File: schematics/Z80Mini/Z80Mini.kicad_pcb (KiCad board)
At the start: 2 copper layers, 194.3 x 105.4 mm, 50 parts, among them J1 Conn_02x20_Odd_Even, J3 USB_B_Micro, J4 Conn_02x10_Counter_Clockwise, SW1 RESET, SW2 SW_DIP_x04, U1 Z80CPU, U2 TC55257CPI, U3 AT28C64B-15PU, U4 74LS32, U5 74HC14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

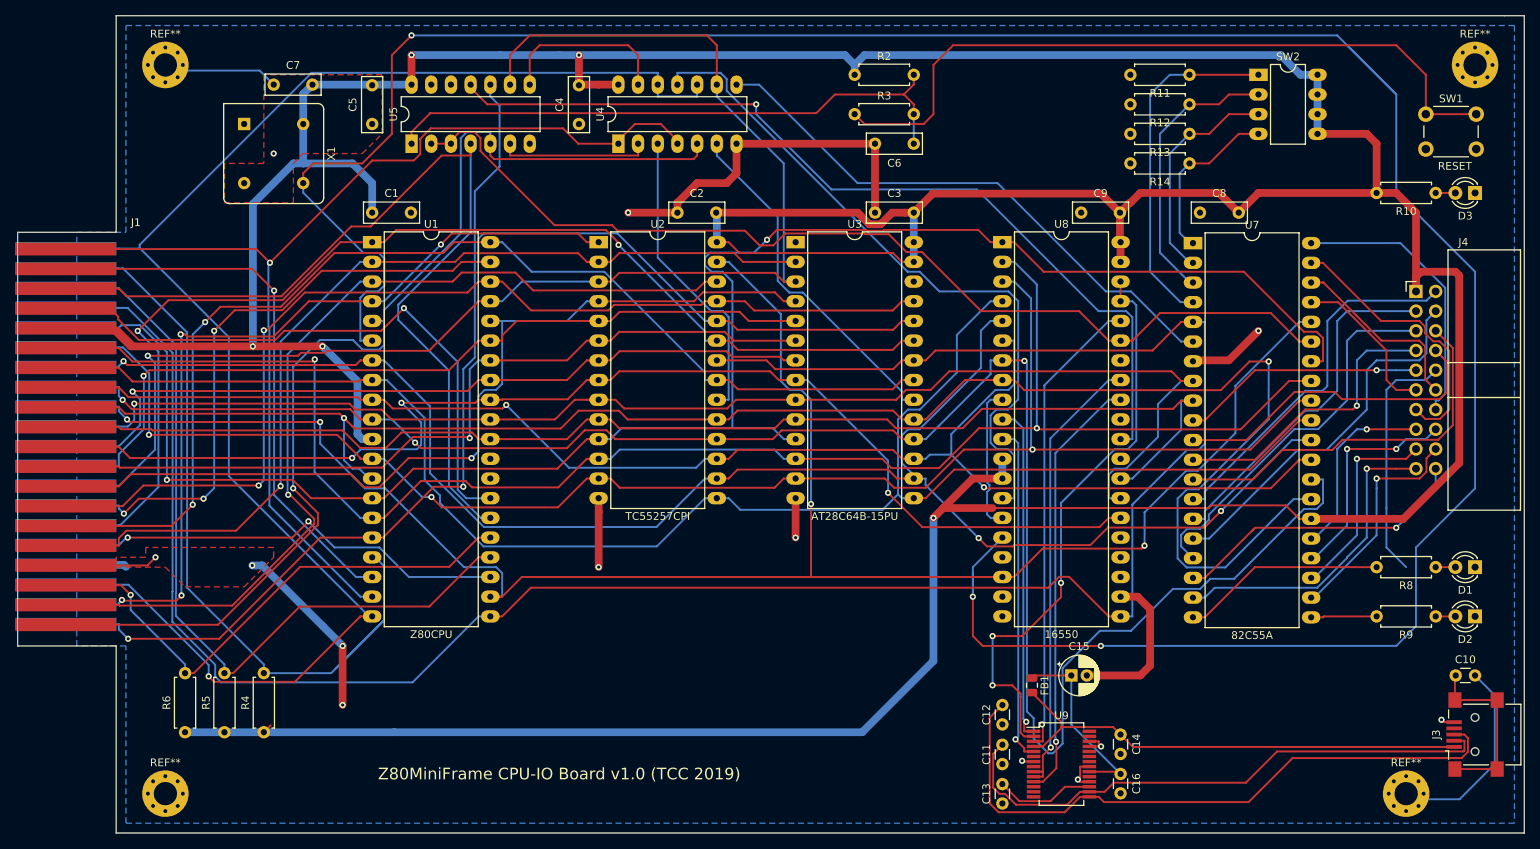
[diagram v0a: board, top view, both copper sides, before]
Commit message: Latest modifications and update to v1.1 and first successifully VDP routines test.
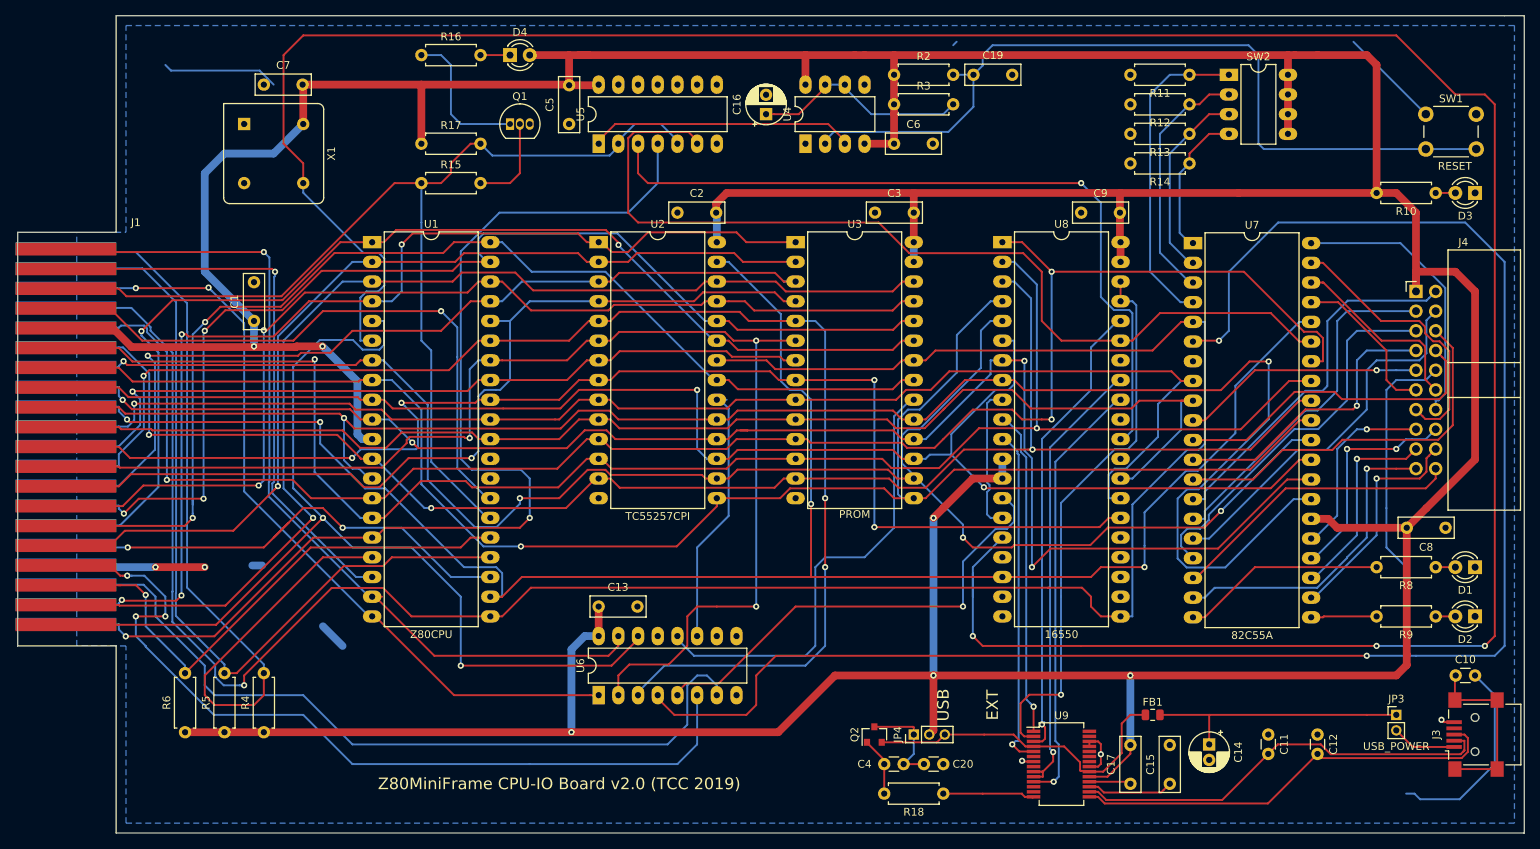
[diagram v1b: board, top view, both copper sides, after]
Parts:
- removed REF** (x4): MountingHole_3mm_Pad_Via, MountingHole:MountingHole_3mm_Pad_Via
- added C17: 100nF, Capacitor_THT:C_Disc_D7.0mm_W2.5mm_P5.00mm, F.Cu at (208.3, 143.5)
- added C19: 100nF, Capacitor_THT:C_Disc_D7.0mm_W2.5mm_P5.00mm, F.Cu at (188.0, 52.1)
- added C20: 0.1uF, Capacitor_THT:C_Disc_D3.0mm_W1.6mm_P2.50mm, F.Cu at (184.2, 141.0)
- added D4: LED, LED_THT:LED_D3.0mm, F.Cu at (128.3, 49.5)
- added JP3: USB_POWER, Connector_PinHeader_2.00mm:PinHeader_1x02_P2.00mm_Vertical, F.Cu at (242.6, 134.6)
- added JP4: SELF_POWER, Connector_PinHeader_2.00mm:PinHeader_1x03_P2.00mm_Vertical, F.Cu at (180.3, 137.2)
- added Q1: BC337, Package_TO_SOT_THT:TO-92_Inline, F.Cu at (128.3, 58.4)
- added Q2: IRLML6402, Package_TO_SOT_SMD:SOT-23, F.Cu at (175.3, 137.2)
- added R15: 1K, Resistor_THT:R_Axial_DIN0207_L6.3mm_D2.5mm_P7.62mm_Horizontal, F.Cu at (116.8, 66.0)
- added R16: 330R, Resistor_THT:R_Axial_DIN0207_L6.3mm_D2.5mm_P7.62mm_Horizontal, F.Cu at (116.8, 49.5)
- added R17: 10K, Resistor_THT:R_Axial_DIN0207_L6.3mm_D2.5mm_P7.62mm_Horizontal, F.Cu at (116.8, 61.0)
- added R18: 1K, Resistor_THT:R_Axial_DIN0207_L6.3mm_D2.5mm_P7.62mm_Horizontal, F.Cu at (184.2, 144.8)
- added U6: 74LS139, Package_DIP:DIP-16_W7.62mm_LongPads, F.Cu at (139.7, 132.1)
- C13: value 0.1 -> 100nF; footprint Capacitor_THT:C_Disc_D3.0mm_W1.6mm_P2.50mm -> Capacitor_THT:C_Disc_D7.0mm_W2.5mm_P5.00mm
- C14: value 0.1 -> 10uF; footprint Capacitor_THT:C_Disc_D3.0mm_W1.6mm_P2.50mm -> Capacitor_THT:CP_Radial_D5.0mm_P2.00mm
- C15: value 10uF -> 100nF; footprint Capacitor_THT:CP_Radial_D5.0mm_P2.00mm -> Capacitor_THT:C_Disc_D7.0mm_W2.5mm_P5.00mm
- C16: value 0.1 -> 10uF; footprint Capacitor_THT:C_Disc_D3.0mm_W1.6mm_P2.50mm -> Capacitor_THT:CP_Radial_D5.0mm_P2.50mm
- C4: value 100nF -> 0.1uF; footprint Capacitor_THT:C_Disc_D7.0mm_W2.5mm_P5.00mm -> Capacitor_THT:C_Disc_D3.0mm_W1.6mm_P2.50mm
- R2: value 10K -> 100K
- R3: value 10 -> 47K
- U3: value AT28C64B-15PU -> 28C256
- U4: value 74LS32 -> NE555; footprint Package_DIP:DIP-14_W7.62mm_LongPads -> Package_DIP:DIP-8_W7.62mm_LongPads
- moved C16 96.6 mm to (161.3, 57.1), turned to 90 degrees
- moved C4 91.5 mm to (176.5, 141.0), turned to 0 degrees
- moved C13 57.9 mm to (139.7, 120.7), turned to 0 degrees
- moved C8 51.5 mm to (248.9, 110.5), turned to 180 degrees
- moved C12 40.7 mm to (232.4, 137.2), turned to 270 degrees
- moved C11 34.5 mm to (226.1, 137.2), turned to 270 degrees
- moved C5 25.4 mm to (135.9, 58.4)
- moved U4 24.1 mm to (166.4, 61.0)
- moved U5 24.1 mm to (139.7, 61.0)
- moved C1 20.7 mm to (95.2, 83.8), turned to 90 degrees
- moved C15 18.9 mm to (213.4, 143.5), turned to 90 degrees
- moved FB1 16.0 mm to (211.2, 134.6), turned to 0 degrees
- moved C14 11.5 mm to (218.4, 138.4)
- moved R3 5.24 mm to (177.8, 55.9)
- moved R2 5.08 mm to (177.8, 52.1)
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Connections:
- C13 pad 1: GND -> +5V
- C13 pad 2: Net-(C13-Pad2) -> GND
- C16 pad 1: Net-(C15-Pad1) -> Net-(C16-Pad1)
- C4 pad 1: GND -> Net-(C4-Pad1)
- C4 pad 2: +5V -> Net-(C20-Pad2)
- C6 pad 1: Net-(C6-Pad1) -> +5V
- FB1 pad 1: Net-(C15-Pad1) -> Net-(FB1-Pad1)
- J1 pad 2: /IORQ -> NMI
- J1 pad 33: GND -> /VDP_SEL
- J1 pad 36: /IORQ -> /SND_SEL
- J1 pad 4: NMI -> WAIT
- J1 pad 6: WAIT -> /IORQ
- J3 pad 1: Net-(C14-Pad1) -> Net-(J3-Pad1)
- R2 pad 2: Net-(C6-Pad1) -> Net-(C19-Pad1)
- R3 pad 1: Net-(R3-Pad1) -> +5V
- R3 pad 2: Net-(C6-Pad1) -> Net-(C16-Pad1)
- SW1 pad 1: Net-(R3-Pad1) -> GND
- SW1 pad 2: GND -> Net-(C19-Pad1)
- U3 pad 1: Net-(U3-Pad1) -> /A14
- U3 pad 26: Net-(U3-Pad26) -> /A13
- U4 pad 1: MREQ -> GND
- U4 pad 2: Net-(U4-Pad2) -> Net-(C19-Pad1)
- U4 pad 3: Net-(U2-Pad20) -> Net-(U4-Pad3)
- U4 pad 4: MREQ -> +5V
- U4 pad 5: /A15 -> Net-(U4-Pad5)
- U4 pad 6: Net-(U3-Pad20) -> Net-(C16-Pad1)
- U4 pad 7: GND -> Net-(C16-Pad1)
- U4 pad 8: /IO_UART/IO_CE -> +5V
- U5 pad 1: Net-(C6-Pad1) -> Net-(U4-Pad3)
- U5 pad 10: /INT -> (no net)
- U5 pad 11: /IO_UART/UART_INTR -> (no net)
- U5 pad 2: IO_RESET -> /RESET
- U5 pad 3: IO_RESET -> /IO_UART/UART_INTR
- U5 pad 4: /RESET -> /INT
- U5 pad 5: /A15 -> /RESET
- U5 pad 6: Net-(U4-Pad2) -> IO_RESET
- U5 pad 8: Net-(U4-Pad13) -> (no net)
- U5 pad 9: /A7 -> (no net)
- U9 pad 17: Net-(C13-Pad2) -> Net-(C15-Pad1)
- U9 pad 19: Net-(U9-Pad19) -> +5V
- U9 pad 20: Net-(C15-Pad1) -> Net-(FB1-Pad1)
- U9 pad 4: Net-(C14-Pad1) -> Net-(FB1-Pad1)
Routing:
- net /IO_UART/IO_CE: track 72.6 -> 219.1 mm, vias 0 -> 2
- net /VDP_SEL: track 0.00 -> 110.1 mm, vias 0 -> 3
- net Net-(C19-Pad1): track 0.00 -> 107.5 mm
- net /SND_SEL: track 0.00 -> 103.9 mm
- net /IORQ: track 204.8 -> 103.8 mm, vias 1 -> 2
- net Net-(R3-Pad1): track 95.3 -> 0.00 mm
- net GND: track 222.1 -> 128.4 mm, vias 13 -> 5
- net Net-(C6-Pad1): track 77.0 -> 0.00 mm
- net /A5: track 108.2 -> 179.8 mm, vias 1 -> 3
- net +5V: track 700.9 -> 768.2 mm, vias 5 -> 6
- net /A7: track 182.0 -> 115.9 mm
- net /A4: track 107.2 -> 168.0 mm, vias 1 -> 3
- net Net-(FB1-Pad1): track 0.00 -> 41.8 mm
- net /D6: track 246.1 -> 204.6 mm, vias 3 -> 4
- net Net-(U4-Pad3): track 0.00 -> 35.1 mm
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- removed copper zone on F.Cu, net GND
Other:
- board text added: "EXT"
- board text added: "PROM"
- board text added: "USB"
- board text added: "Z80MiniFrame CPU-IO Board v2.0 (TCC 2019)"
- board text removed: "Z80MiniFrame CPU-IO Board v1.0 (TCC 2019)"

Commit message: Added new code for core written in C with Z88DK
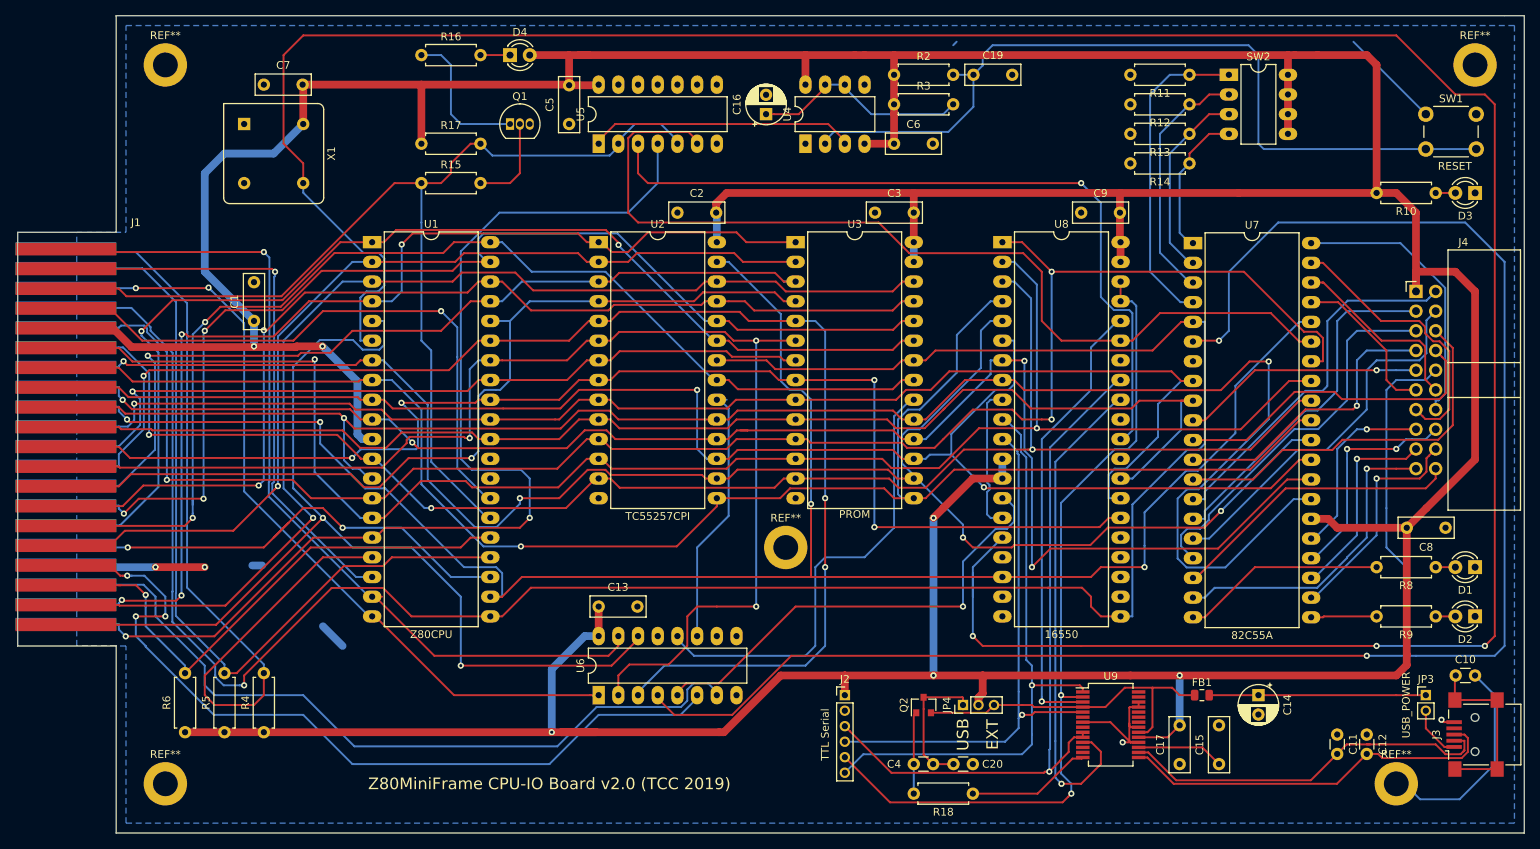
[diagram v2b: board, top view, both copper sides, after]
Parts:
- added J2: TTL Serial, Connector_PinHeader_2.00mm:PinHeader_1x06_P2.00mm_Vertical, F.Cu at (171.4, 132.1)
- added REF**: MountingHole_3.2mm_M3_DIN965_Pad, MountingHole:MountingHole_3.2mm_M3_DIN965_Pad, F.Cu at (163.8, 113.0)
- added REF**: MountingHole_3.2mm_M3_DIN965_Pad, MountingHole:MountingHole_3.2mm_M3_DIN965_Pad, F.Cu at (242.6, 143.5)
- added REF**: MountingHole_3.2mm_M3_DIN965_Pad, MountingHole:MountingHole_3.2mm_M3_DIN965_Pad, F.Cu at (83.8, 143.5)
- added REF**: MountingHole_3.2mm_M3_DIN965_Pad, MountingHole:MountingHole_3.2mm_M3_DIN965_Pad, F.Cu at (83.8, 50.8)
- added REF**: MountingHole_3.2mm_M3_DIN965_Pad, MountingHole:MountingHole_3.2mm_M3_DIN965_Pad, F.Cu at (252.7, 50.8)
- C14: footprint Capacitor_THT:CP_Radial_D5.0mm_P2.00mm -> Capacitor_THT:CP_Radial_D5.0mm_P2.50mm
- moved C14 8.98 mm to (224.8, 132.1)
- moved C11 8.89 mm to (234.9, 137.2)
- moved U9 8.13 mm to (205.7, 135.9)
- moved Q2 7.41 mm to (181.6, 133.3)
- moved JP4 7.41 mm to (186.7, 133.3)
- moved C15 6.84 mm to (219.7, 141.0)
- moved C17 6.84 mm to (214.6, 141.0)
- moved FB1 6.84 mm to (217.5, 132.1)
- moved C12 6.35 mm to (238.8, 137.2)
- moved JP3 4.58 mm to (246.4, 132.1)
- moved C20 3.81 mm to (188.0, 141.0)
- moved C4 3.81 mm to (180.3, 141.0)
- moved R18 3.81 mm to (188.0, 144.8)
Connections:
- net Net-(U8-Pad10) renamed /RX
- net Net-(U8-Pad11) renamed /TX
- net Net-(U8-Pad33) renamed /DTR
- net Net-(U8-Pad37) renamed /DSR
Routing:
- net /DSR: track 71.4 -> 108.2 mm, vias 1 -> 2
- net /RX: track 42.1 -> 76.6 mm
- net /DTR: track 58.3 -> 91.0 mm
- net /TX: track 44.2 -> 70.1 mm
- net GND: track 128.4 -> 120.3 mm, vias 5 -> 4
- net Net-(U8-Pad32): track 56.1 -> 64.1 mm
- net Net-(C12-Pad2): track 56.8 -> 49.8 mm
- net Net-(C14-Pad1): track 34.3 -> 27.9 mm
- net Net-(C11-Pad2): track 55.3 -> 49.3 mm
- net Net-(C20-Pad2): track 13.0 -> 18.3 mm
- net Net-(R18-Pad1): track 12.0 -> 16.7 mm
- net Net-(C4-Pad1): track 7.54 -> 11.2 mm
- net /VDP_SEL: track 110.1 -> 106.6 mm
- net /SND_SEL: track 103.9 -> 100.6 mm
- net /IO_UART/IO_CE: track 219.1 -> 216.8 mm
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
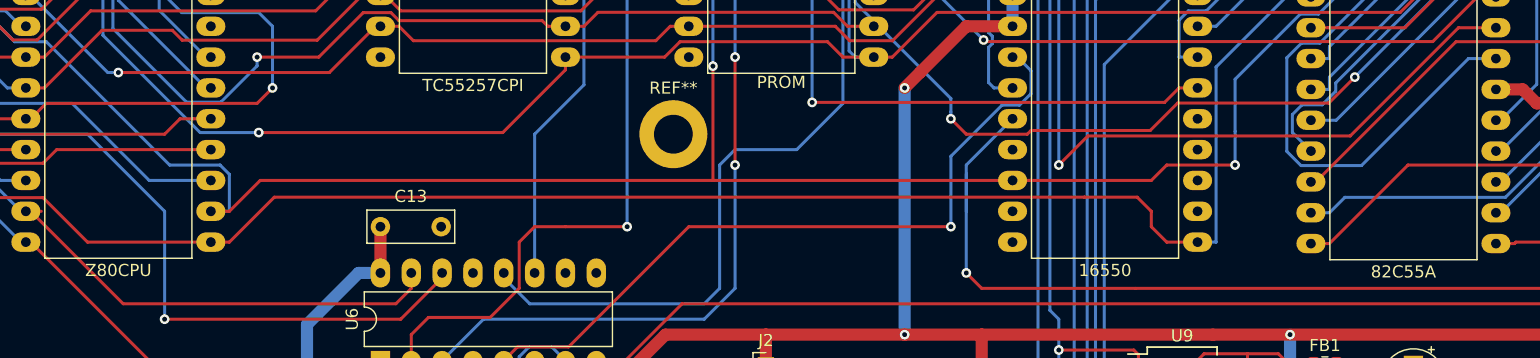
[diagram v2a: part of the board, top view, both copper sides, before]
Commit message: Testing C routines for VDP and keyboard. Generated backplane gerber files
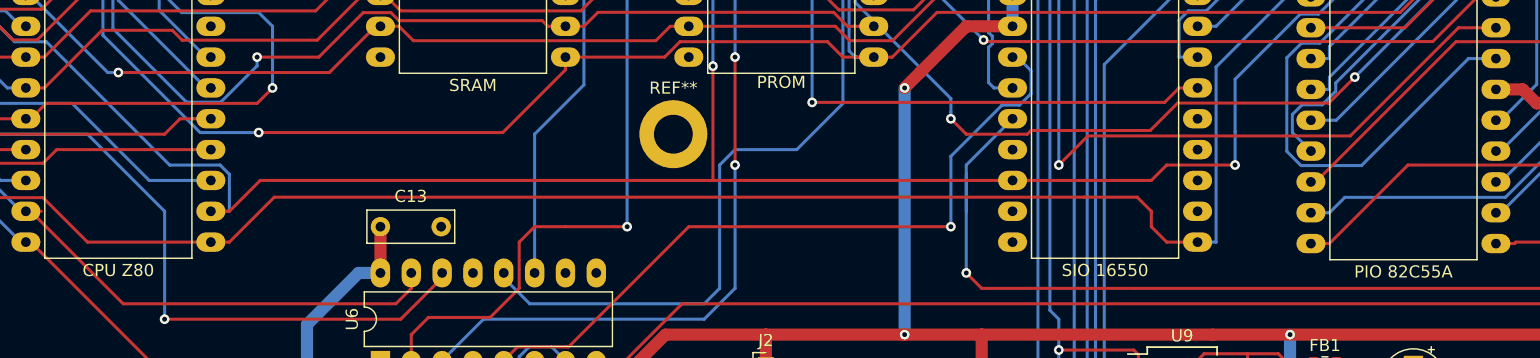
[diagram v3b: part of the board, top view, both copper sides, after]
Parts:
- U1: value Z80CPU -> CPU Z80
- U2: value TC55257CPI -> SRAM
- U7: value 82C55A -> PIO 82C55A
- U8: value 16550 -> SIO 16550
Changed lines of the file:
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@@
       (effects (font (size 1 1) (thickness 0.15)))
     )
-    (fp_text value Z80CPU (at 7.62 50.59) (layer F.SilkS)
+    (fp_text value "CPU Z80" (at 7.62 50.59) (layer F.SilkS)
       (effects (font (size 1 1) (thickness 0.15)))
     )
@@
       (effects (font (size 1 1) (thickness 0.15)))
     )
-    (fp_text value TC55257CPI (at 7.62 35.35) (layer F.SilkS)
+    (fp_text value SRAM (at 7.62 35.35) (layer F.SilkS)
       (effects (font (size 1 1) (thickness 0.15)))
     )
@@
       (effects (font (size 1 1) (thickness 0.15)))
     )
-    (fp_text value 16550 (at 7.62 50.59) (layer F.SilkS)
+    (fp_text value "SIO 16550" (at 7.62 50.59) (layer F.SilkS)
       (effects (font (size 1 1) (thickness 0.15)))
     )
@@
       (effects (font (size 1 1) (thickness 0.15)))
     )
-    (fp_text value 82C55A (at 7.62 50.59) (layer F.SilkS)
-      (effects (font (size 1 1) (thickness 0.15)))
-    )
+    (fp_text value "PIO 82C55A" (at 7.62 50.59) (layer F.SilkS)
+      (effects (font (size 1 1) (thickness 0.15)))
+    )
